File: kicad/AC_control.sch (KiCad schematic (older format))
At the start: 17 parts, among them J4 HAG Resistor, J5 PWR_IN, J6 PWR_Suply, Q2 Q_PNP_CBE, U2 MOC3023M

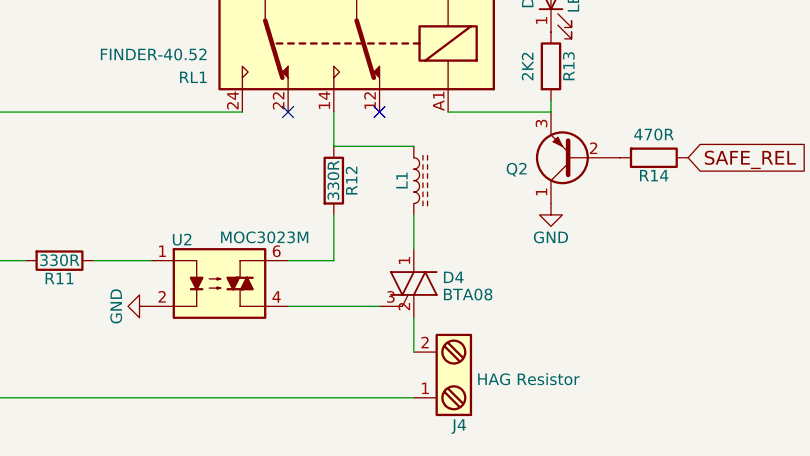
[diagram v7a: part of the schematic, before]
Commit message: Update with new PCB version
Kicad schematic and pcb layout correction on Mosfet and Triac footprint.
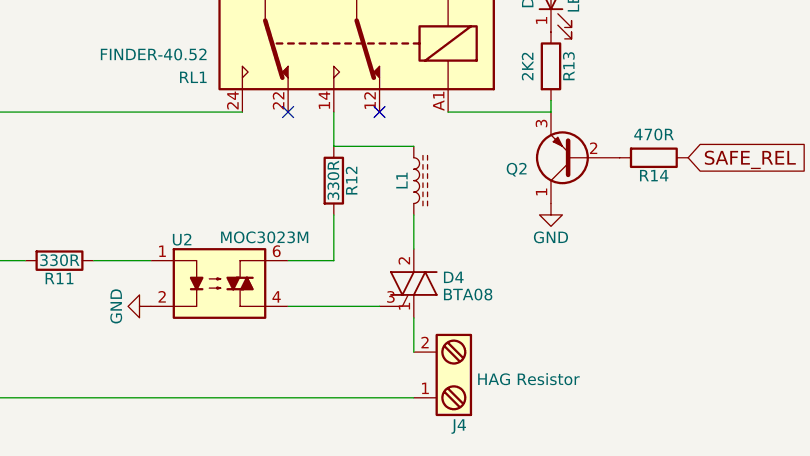
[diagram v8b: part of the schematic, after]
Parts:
- removed D4: BTA08, TO_SOT_Packages_THT:TO-220_Vertical, symbol Q_TRIAC_AAG
- added D4: BTA08, TO_SOT_Packages_THT:TO-220_Neutral123_Vertical, symbol Q_TRIAC_AAG-2
- L1: footprint Inductors_THT:L_Toroid_Vertical_L16.0mm_W8.0mm_P7.62mm -> Choke_SMD:Choke_SMD_PISR_Handsoldering_FASTRON
- R10: footprint Resistors_THT:R_Axial_DIN0411_L9.9mm_D3.6mm_P15.24mm_Horizontal -> Discret:D4
- R11: footprint Resistors_SMD:R_0603_HandSoldering -> Resistors_ThroughHole:Resistor_Horizontal_RM7mm
- R12: footprint Resistors_THT:R_Axial_DIN0309_L9.0mm_D3.2mm_P12.70mm_Horizontal -> Discret:R3
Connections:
- net at U2.4: now also D4.3 (G)
- net at L1.2: now also D4.2 (A2)
- net at J4.2: now also D4.1 (A1)
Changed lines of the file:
@@
 F 0 "R12" V 4380 4600 50  0000 C CNN
 F 1 "330R" V 4300 4600 50  0000 C CNN
-F 2 "Resistors_THT:R_Axial_DIN0309_L9.0mm_D3.2mm_P12.70mm_Horizontal" V 4230 4600 50  0001 C CNN
+F 2 "Discret:R3" V 4230 4600 50  0001 C CNN
 F 3 "" H 4300 4600 50  0000 C CNN
 	1    4300 4600
@@
 F 0 "L1" V 4600 4600 50  0000 C CNN
 F 1 "L_Core_Ferrite" V 4760 4600 50  0001 C CNN
-F 2 "Inductors_THT:L_Toroid_Vertical_L16.0mm_W8.0mm_P7.62mm" H 4650 4600 50  0001 C CNN
+F 2 "Choke_SMD:Choke_SMD_PISR_Handsoldering_FASTRON" H 4650 4600 50  0001 C CNN
 F 3 "" H 4650 4600 50  0000 C CNN
 	1    4650 4600
-	1    0    0    -1
-$EndComp
-$Comp
-L Q_TRIAC_AAG D4
-U 1 1 5A0A5335
-P 4650 5050
-F 0 "D4" H 4775 5075 50  0000 L CNN
-F 1 "BTA08" H 4775 5000 50  0000 L CNN
-F 2 "TO_SOT_Packages_THT:TO-220_Vertical" V 4725 5075 50  0001 C CNN
-F 3 "" V 4650 5050 50  0000 C CNN
-	1    4650 5050
 	1    0    0    -1
 $EndComp
@@
 F 0 "R11" V 3180 4950 50  0000 C CNN
 F 1 "330R" V 3100 4950 50  0000 C CNN
-F 2 "Resistors_SMD:R_0603_HandSoldering" V 3030 4950 50  0001 C CNN
+F 2 "Resistors_ThroughHole:Resistor_Horizontal_RM7mm" V 3030 4950 50  0001 C CNN
 F 3 "" H 3100 4950 50  0000 C CNN
 	1    3100 4950
@@
 F 0 "R10" V 3130 2000 50  0000 C CNN
 F 1 "100k" V 3050 2000 50  0000 C CNN
-F 2 "Resistors_THT:R_Axial_DIN0411_L9.9mm_D3.6mm_P15.24mm_Horizontal" V 2980 2000 50  0001 C CNN
+F 2 "Discret:D4" V 2980 2000 50  0001 C CNN
 F 3 "" H 3050 2000 50  0001 C CNN
 	1    3050 2000
@@
 Wire Wire Line
 	4400 3400 4400 3700
+$Comp
+L Q_TRIAC_AAG-2 D4
+U 1 1 5C673880
+P 4650 5050
+F 0 "D4" H 4775 5075 50  0000 L CNN
+F 1 "BTA08" H 4775 5000 50  0000 L CNN
+F 2 "TO_SOT_Packages_THT:TO-220_Neutral123_Vertical" V 4725 5075 50  0001 C CNN
+F 3 "" V 4650 5050 50  0000 C CNN
+	1    4650 5050
+	1    0    0    -1
+$EndComp
 $EndSCHEMATC
